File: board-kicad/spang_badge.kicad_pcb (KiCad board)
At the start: 2 copper layers, 37.5 x 43.5 mm, 19 parts, among them IC1 ATTINY20-X, J1 CONN-TAGCONNECT-TC2050, Q1 Q_NMOS_GSD, SW1 SW_SPST

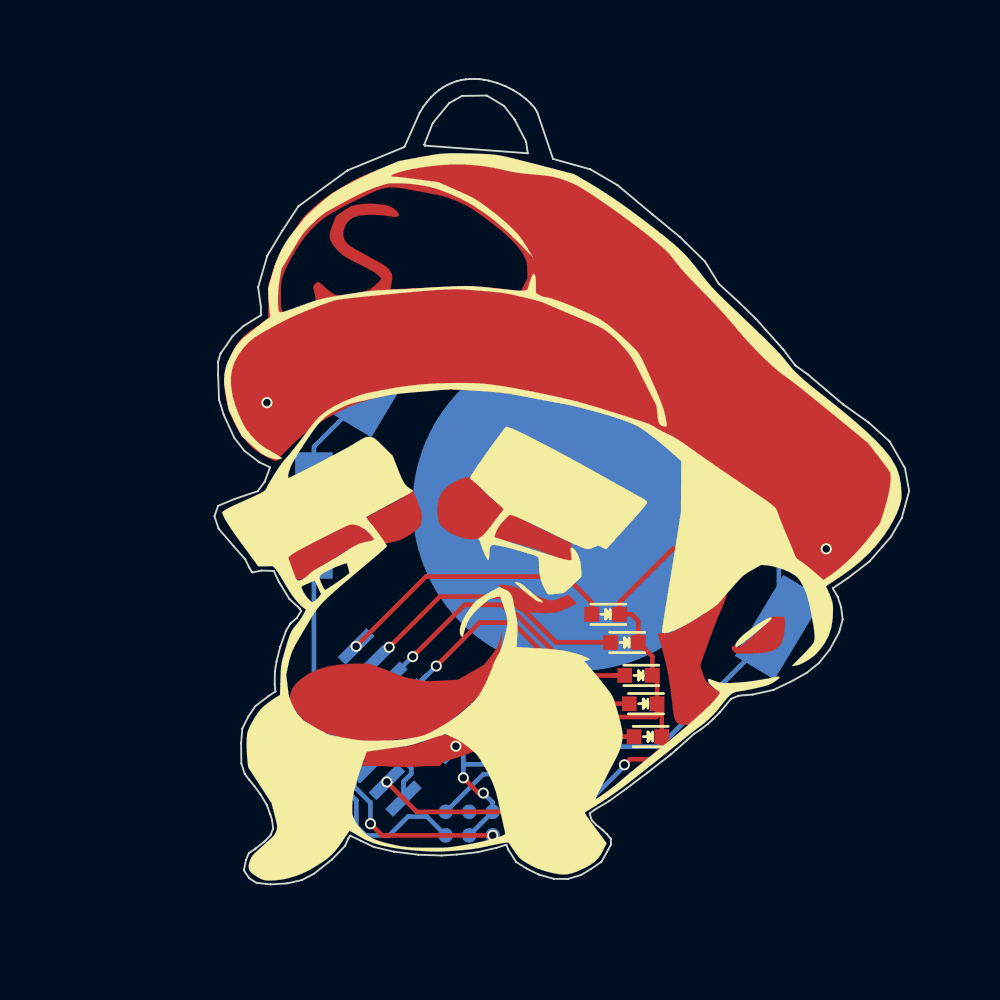
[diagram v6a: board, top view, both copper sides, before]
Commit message: working on spang badge v2. TODO: fix B-CU
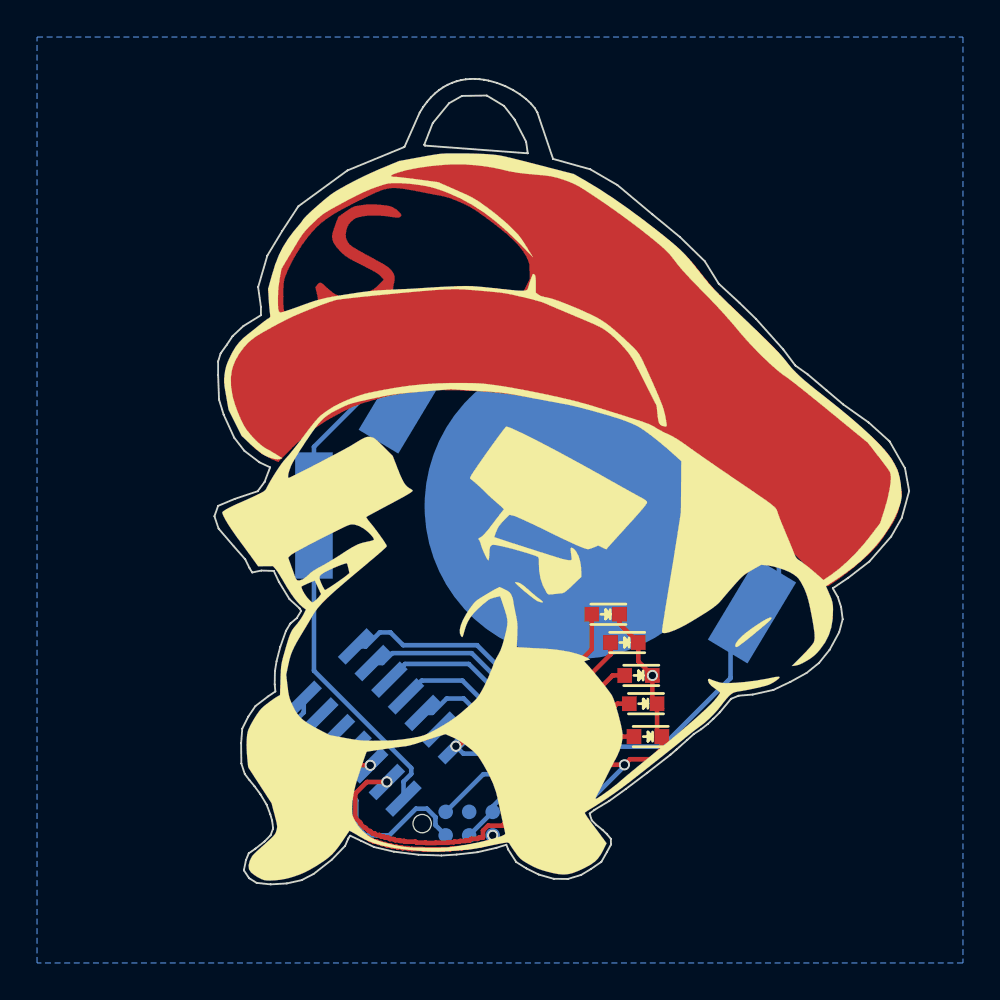
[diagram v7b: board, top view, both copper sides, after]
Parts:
- removed the G*** at (135.2, 86.2)
- removed the G*** at (182.4, 126.5) (x3)
- added G*** (x2): LOGO, LOGO, F.Cu at (182.4, 126.5)
- added G***: LOGO, spang_badge:LOGO, F.Cu at (182.5, 126.5)
- J1: footprint spang_badge:TC2050_IDC -> spang_badge:TC2050-All_Holes
- R1, R2: footprint Resistors_SMD:R_0603 -> Resistors_SMD:R_0603_HandSoldering
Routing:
- net GND: track 108.4 -> 89.4 mm, vias 7 -> 6
- net /TCK: track 7.65 -> 14.4 mm
- net +BATT: track 77.9 -> 83.0 mm
- net /TDI: track 10.7 -> 13.5 mm
- net Net-(D4-Pad2): track 17.1 -> 14.9 mm
- net (no net): track 1.51 -> 0.00 mm
- net Net-(D3-Pad2): track 16.6 -> 15.2 mm
- net Net-(D5-Pad2): track 12.7 -> 13.9 mm
- net Net-(D1-Pad2): track 15.5 -> 16.3 mm
- net Net-(D2-Pad2): track 15.4 -> 16.0 mm
- net /nRST: track 10.8 -> 11.4 mm
- added copper zone on B.Cu, net GND

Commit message: workin on cryptid shroom
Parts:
- removed the G*** at (182.4, 126.5) (x2)
- added G*** (x2): LOGO, LOGO, F.Cu at (182.4, 126.5)
- moved D8 0.54 mm to (143.9, 89.4), turned to 189 degrees
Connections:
- J1 pad 1: +BATT -> /TCK
- J1 pad 10: /nRST -> Net-(J1-Pad10)
- J1 pad 2: Net-(J1-Pad2) -> GND
- J1 pad 3: GND -> /TDI
- J1 pad 4: /TCK -> +BATT
- J1 pad 5: GND -> Net-(J1-Pad5)
- J1 pad 6: Net-(J1-Pad6) -> /nRST
- J1 pad 8: /TDI -> Net-(J1-Pad8)
- J1 pad 9: GND -> Net-(J1-Pad9)
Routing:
- net /nRST: track 11.4 -> 17.7 mm, vias 0 -> 2
- net GND: track 89.4 -> 83.3 mm, vias 6 -> 8
- net /TCK: track 14.4 -> 10.7 mm
- net +BATT: track 83.0 -> 79.8 mm
- net Net-(D8-Pad1): track 2.13 -> 3.90 mm
- net /TDI: track 13.5 -> 14.6 mm
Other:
- board text added: "JLCJLCJLCJLC"
